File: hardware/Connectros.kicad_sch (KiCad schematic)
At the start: 7 parts, among them J1 Signals, J2 Diagnostics, J3 Power & CAN

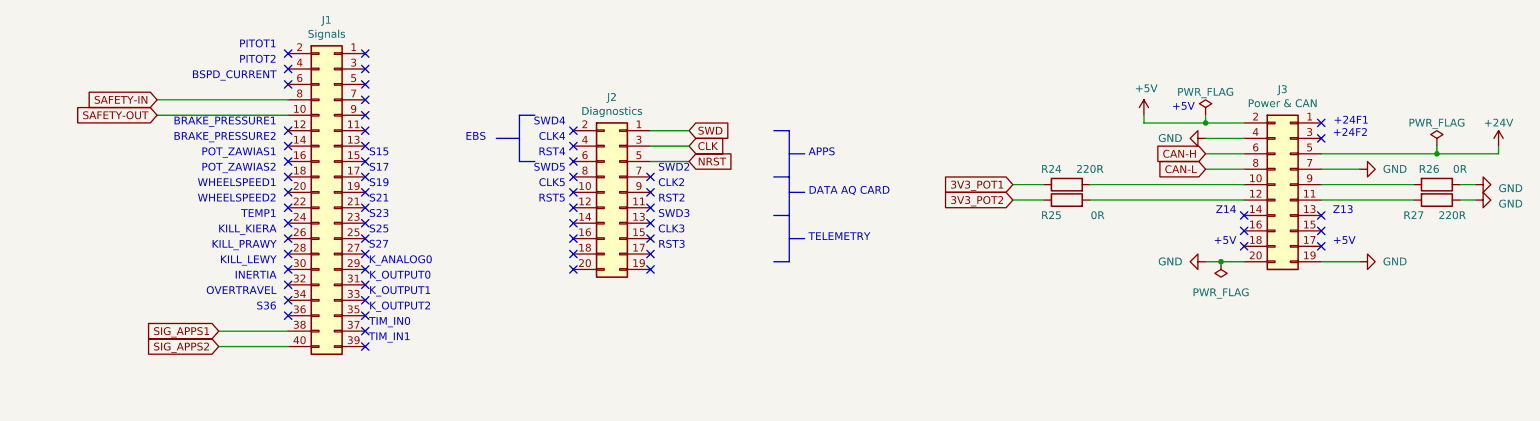
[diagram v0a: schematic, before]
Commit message: Add brake pressure sensors
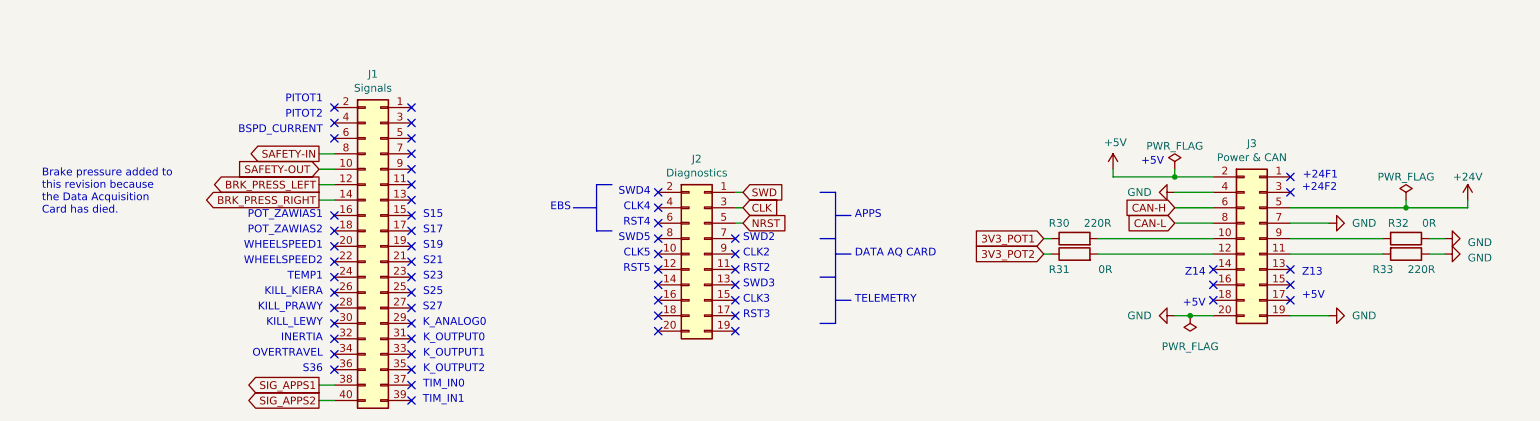
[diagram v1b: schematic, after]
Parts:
- renumbered R24 to R30, R25 to R31, R26 to R32, R27 to R33
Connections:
- net BRK_PRESS_LEFT: now reaches J1.12 (Pin_12)
- net BRK_PRESS_RIGHT: now reaches J1.14 (Pin_14)
- no-connect marks 61 -> 59
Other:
- note removed: "BRAKE_PRESSURE1"
- note removed: "BRAKE_PRESSURE2"
- moved on the sheet: J1, J2, J3, R30, R31, R32, R33

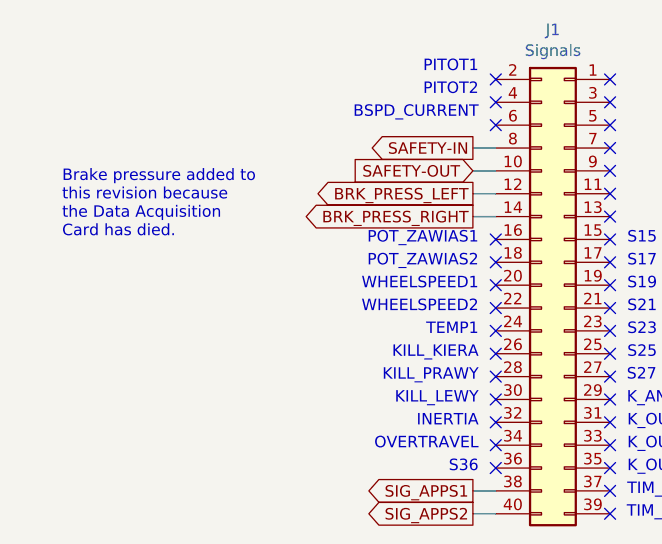
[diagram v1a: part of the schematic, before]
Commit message: Add 0R resistors to the brake pressure signals
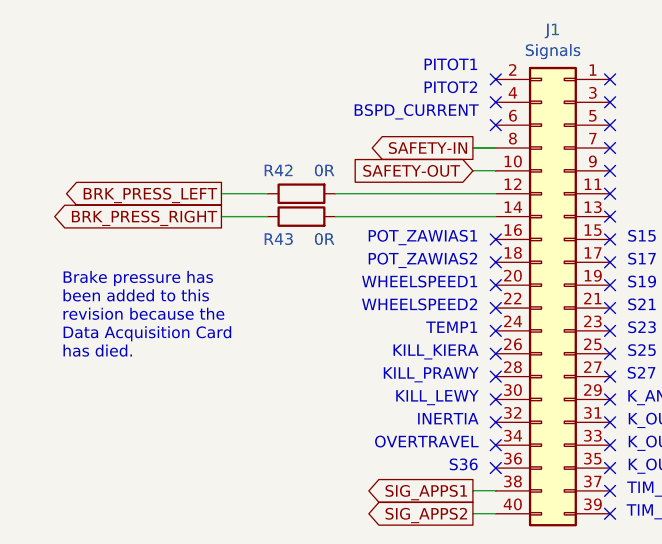
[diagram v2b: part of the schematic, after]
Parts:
- added R42, R43: 0R, Resistor_SMD:R_0603_1608Metric_Pad0.98x0.95mm_HandSolder, symbol Device:R
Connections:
- net BRK_PRESS_LEFT: now also R42.1; no longer J1.12 (Pin_12)
- net BRK_PRESS_RIGHT: now also R43.1; no longer J1.14 (Pin_14)
- new net: J1.14 (Pin_14), R43.2
- new net: J1.12 (Pin_12), R42.2
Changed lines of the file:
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@@
+    (stroke (width 0) (type default))
+  )
+  (wire (pts (xy 57.15 92.71) (xy 74.93 92.71))
     (stroke (width 0) (type default))
   )
@@
     (stroke (width 0) (type default))
   )
-  (wire (pts (xy 72.39 90.17) (xy 74.93 90.17))
+  (wire (pts (xy 44.45 90.17) (xy 49.53 90.17))
     (stroke (width 0) (type default))
   )
@@
     (stroke (width 0) (type default))
   )
-  (wire (pts (xy 72.39 92.71) (xy 74.93 92.71))
+  (wire (pts (xy 44.45 92.71) (xy 49.53 92.71))
     (stroke (width 0) (type default))
   )
@@
     (stroke (width 0) (type default))
   )
+  (wire (pts (xy 57.15 90.17) (xy 74.93 90.17))
+    (stroke (width 0) (type default))
+  )
   (polyline (pts (xy 157.48 99.06) (xy 154.94 99.06))
     (stroke (width 0) (type default))
@@
     (stroke (width 0) (type default))
   )
-  (text_box "Brake pressure added to this revision because the Data Acquisition Card has died."
-    (at 25.7175 86.2805 0) (size 26.3525 10.2395)
+  (text_box "Brake pressure has been added to this revision because the Data Acquisition Card has died."
+    (at 25.7175 97.7105 0) (size 23.8125 11.5095)
     (stroke (width -0.0001) (type default))
     (fill (type none))
@@
     )
   )
-  (global_label "BRK_PRESS_LEFT" (shape output) (at 72.39 90.17 180) (fields_autoplaced)
-    (effects (font (size 1.27 1.27)) (justify right))
-    (property "Intersheetrefs" "${INTERSHEET_REFS}" (at 54.0519 90.17 0)
+  (global_label "BRK_PRESS_LEFT" (shape output) (at 44.45 90.17 180) (fields_autoplaced)
+    (effects (font (size 1.27 1.27)) (justify right))
+    (property "Intersheetrefs" "${INTERSHEET_REFS}" (at 26.1119 90.17 0)
       (effects (font (size 1.27 1.27)) (justify right) hide)
     )
@@
     )
   )
-  (global_label "BRK_PRESS_RIGHT" (shape output) (at 72.39 92.71 180) (fields_autoplaced)
-    (effects (font (size 1.27 1.27)) (justify right))
-    (property "Intersheetrefs" "${INTERSHEET_REFS}" (at 52.8423 92.71 0)
+  (global_label "BRK_PRESS_RIGHT" (shape output) (at 44.45 92.71 180) (fields_autoplaced)
+    (effects (font (size 1.27 1.27)) (justify right))
+    (property "Intersheetrefs" "${INTERSHEET_REFS}" (at 24.9023 92.71 0)
       (effects (font (size 1.27 1.27)) (justify right) hide)
     )
@@
     )
   )
+  (symbol (lib_id "Device:R") (at 53.34 92.71 90) (unit 1)
+    (in_bom yes) (on_board yes) (dnp no)
+    (property "Reference" "R43" (at 50.8 95.25 90)
+      (effects (font (size 1.27 1.27)))
+    )
+    (property "Value" "0R" (at 55.88 95.25 90)
+      (effects (font (size 1.27 1.27)))
+    )
+    (property "Footprint" "Resistor_SMD:R_0603_1608Metric_Pad0.98x0.95mm_HandSolder" (at 53.34 94.488 90)
+      (effects (font (size 1.27 1.27)) hide)
+    )
+    (property "Datasheet" "~" (at 53.34 92.71 0)
+      (effects (font (size 1.27 1.27)) hide)
+    )
+    (pin "1")
+    (pin "2")
+    (instances
+      (project "APPS"
+        (path "/fc4ad874-c922-4070-89f9-7262080469d8/00000000-0000-0000-0000-00006077b773"
+          (reference "R43") (unit 1)
+        )
+      )
+    )
+  )
   (symbol (lib_id "power:+24V") (at 261.62 92.71 0) (unit 1)
     (in_bom yes) (on_board yes) (dnp no) (fields_autoplaced)
@@
         )
       )
+    )
+  )
+  (symbol (lib_id "Device:R") (at 53.34 90.17 90) (mirror x) (unit 1)
+    (in_bom yes) (on_board yes) (dnp no)
+    (property "Reference" "R42" (at 50.8 87.63 90)
+      (effects (font (size 1.27 1.27)))
+    )
+    (property "Value" "0R" (at 55.88 87.63 90)
+      (effects (font (size 1.27 1.27)))
+    )
+    (property "Footprint" "Resistor_SMD:R_0603_1608Metric_Pad0.98x0.95mm_HandSolder" (at 53.34 88.392 90)
+      (effects (font (size 1.27 1.27)) hide)
+    )
+    (property "Datasheet" "~" (at 53.34 90.17 0)
+      (effects (font (size 1.27 1.27)) hide)
+    )
+    (pin "1")
+    (pin "2")
+    (instances
+      (project "APPS"
+        (path "/fc4ad874-c922-4070-89f9-7262080469d8/00000000-0000-0000-0000-00006077b773"
+          (reference "R42") (unit 1)
+        )
+      )
